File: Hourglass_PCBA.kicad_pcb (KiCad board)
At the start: 2 copper layers, 40.9 x 87.5 mm, 152 parts, among them J1 B2B-PH-SM4-TBLFSN, J2 UJ31-CH-G2-SMT-TR, J3 009159010061911, SW1 KMR221NGLFS, U1 STM32L432KCUx, U2 LP5860, U3 LSM6DSOXTR, U4 MCP1727T-3302E/SN, U5 BQ25185DLHR

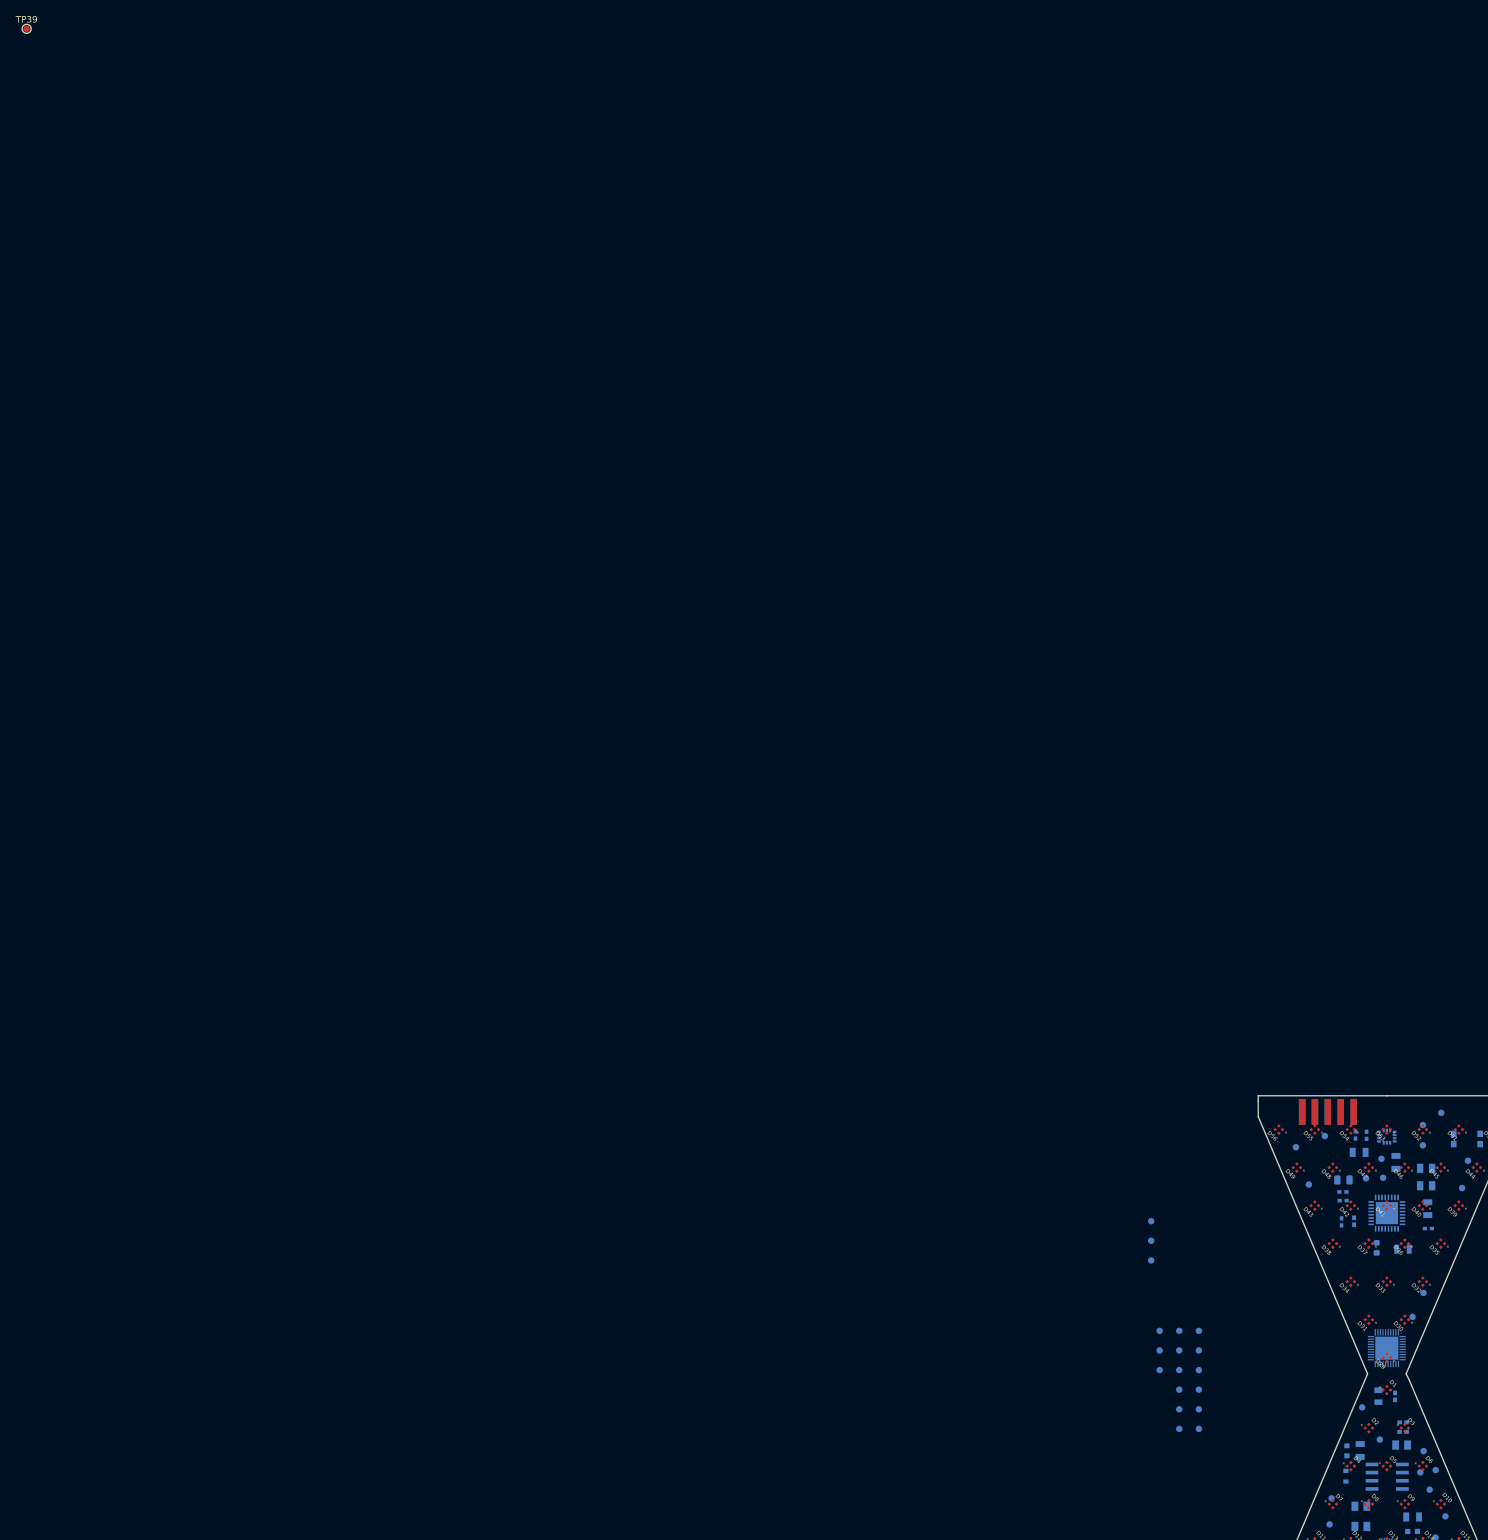
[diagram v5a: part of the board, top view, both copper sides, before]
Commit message: Updated the 3D models
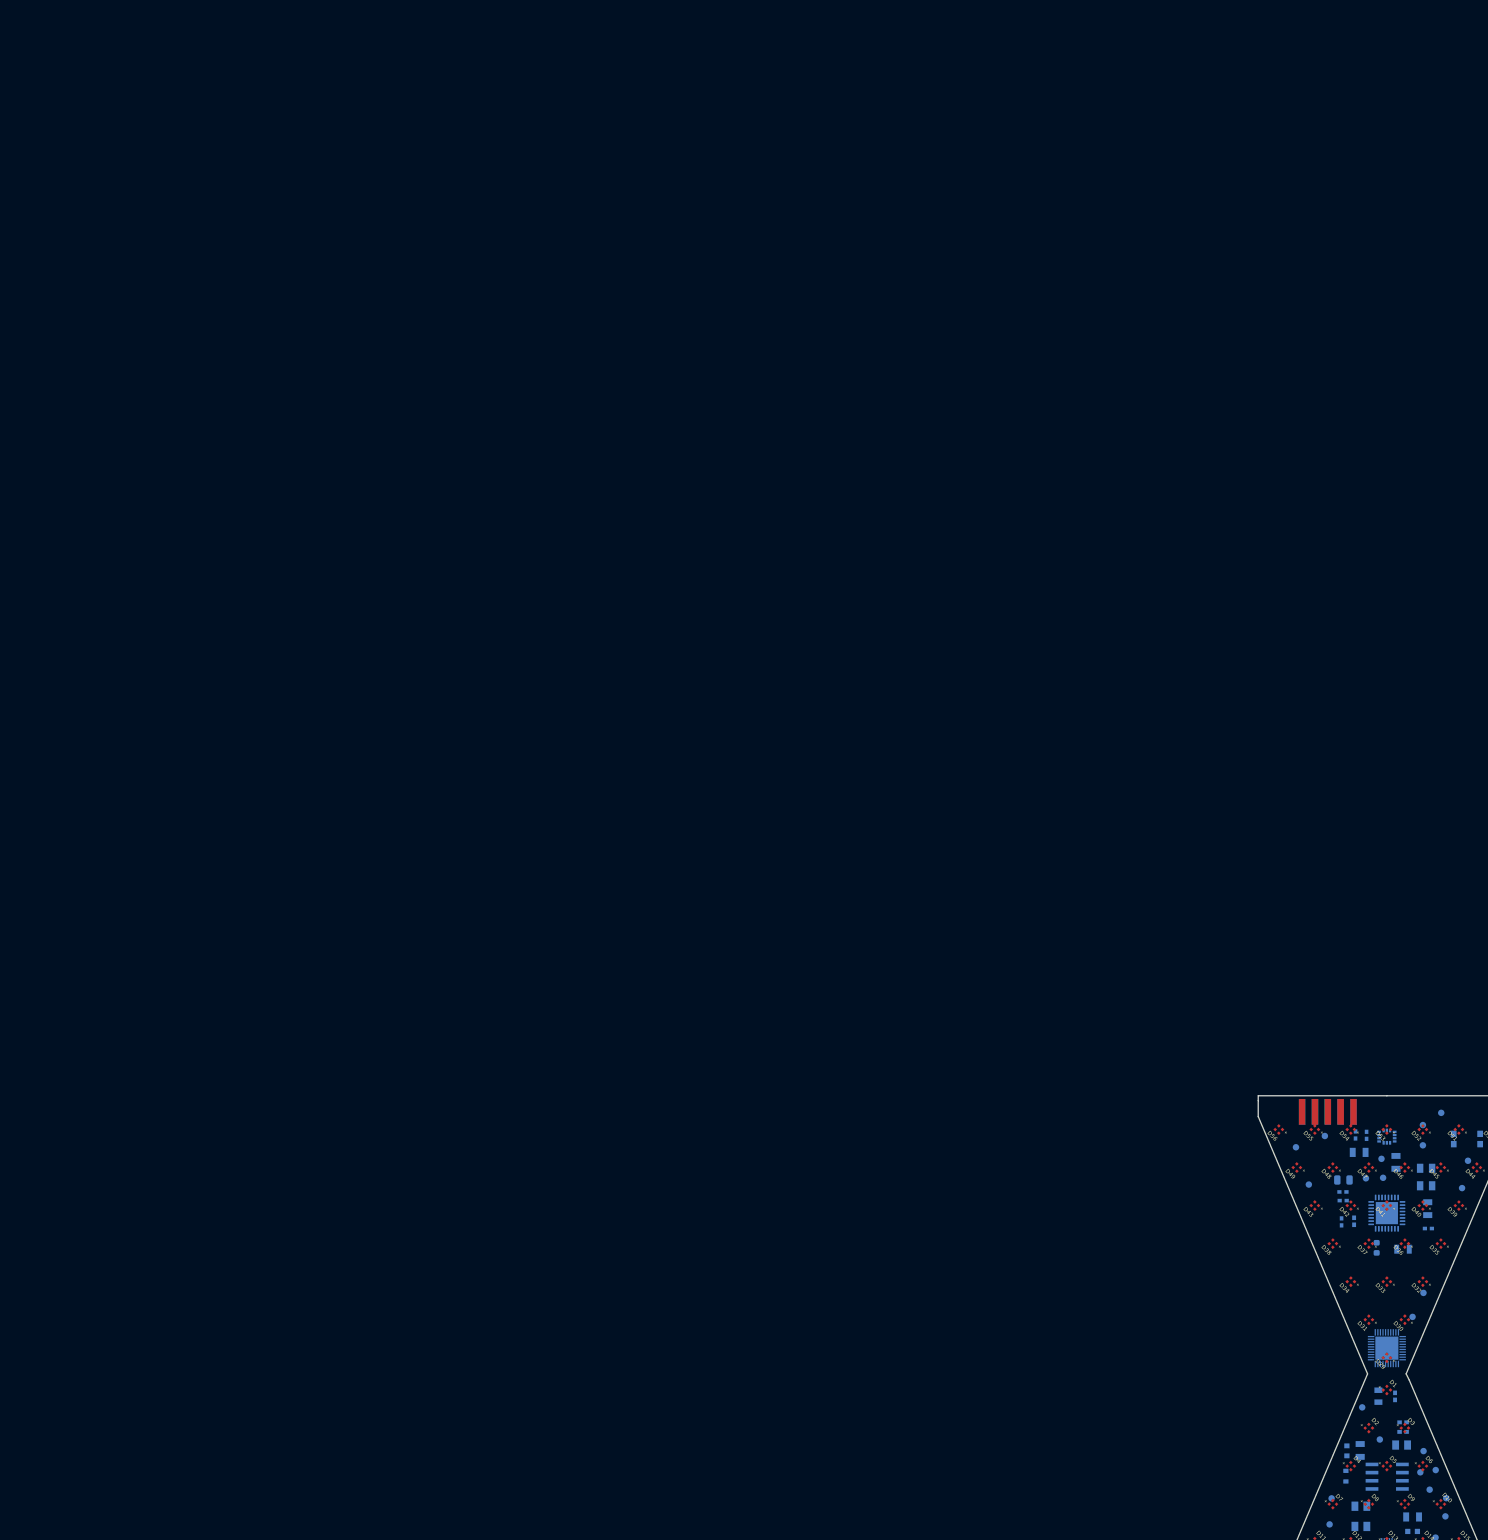
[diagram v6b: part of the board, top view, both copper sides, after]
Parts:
- removed TP10, TP11, TP12, TP13, TP14, TP15, TP16, TP17, TP18, TP19, TP20, TP21, TP22, TP23, TP6, TP7, TP8, TP9: TestPoint, TestPoint:TestPoint_Pad_D1.0mm
- TP39: moved to B.Cu
- moved TP39 317.7 mm to (209.2, 219.3)

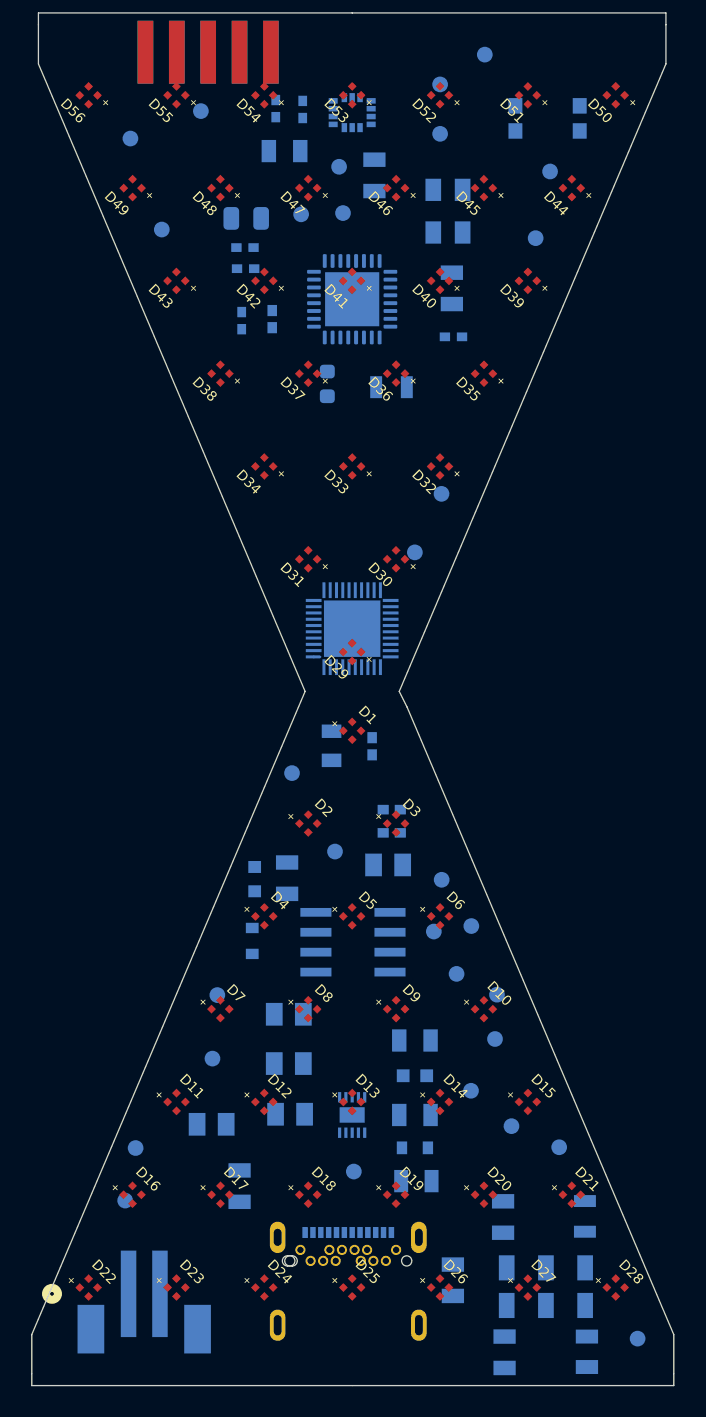
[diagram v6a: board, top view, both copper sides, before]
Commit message: Started routing all of the SW sides.
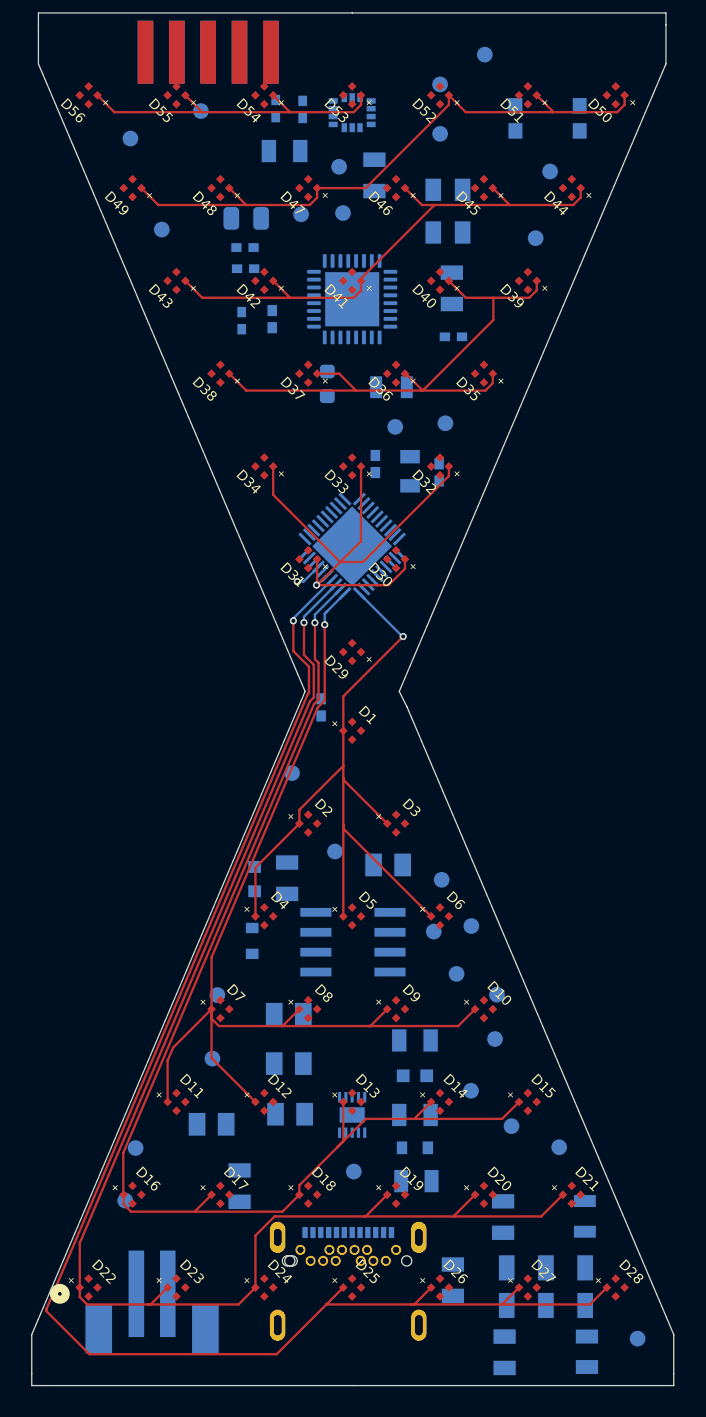
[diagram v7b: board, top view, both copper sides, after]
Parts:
- moved C7 21.7 mm to (205.5, 186.0), turned to 90 degrees
- moved C9 18.2 mm to (203.7, 186.0), turned to 90 degrees
- moved C10 18.0 mm to (201.5, 185.5), turned to 90 degrees
- moved C8 9.18 mm to (198.0, 201.0), turned to -90 degrees
- moved TP1 8.10 mm to (202.7, 183.1)
- moved U2 5.25 mm to (200.0, 190.8), turned to 135 degrees
- moved TP29 4.51 mm to (205.9, 182.9)
- moved J1 0.50 mm to (187.2, 239.6)
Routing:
- net /LED Driver +  LEDs/SW4: track 0.00 -> 94.9 mm, vias 0 -> 1
- net /LED Driver +  LEDs/SW3: track 0.00 -> 91.1 mm, vias 0 -> 1
- net /LED Driver +  LEDs/SW2: track 0.00 -> 77.3 mm, vias 0 -> 1
- net /LED Driver +  LEDs/SW1: track 0.00 -> 64.4 mm, vias 0 -> 1
- net /LED Driver +  LEDs/SW0: track 0.00 -> 47.5 mm, vias 0 -> 1
- net /LED Driver +  LEDs/SW8: track 0.00 -> 39.1 mm
- net /LED Driver +  LEDs/SW6: track 0.00 -> 38.9 mm, vias 0 -> 1
- net /LED Driver +  LEDs/SW5: track 0.00 -> 35.7 mm, vias 0 -> 1
- net /LED Driver +  LEDs/SW7: track 0.00 -> 34.7 mm
- net /LED Driver +  LEDs/SW9: track 0.00 -> 21.1 mm

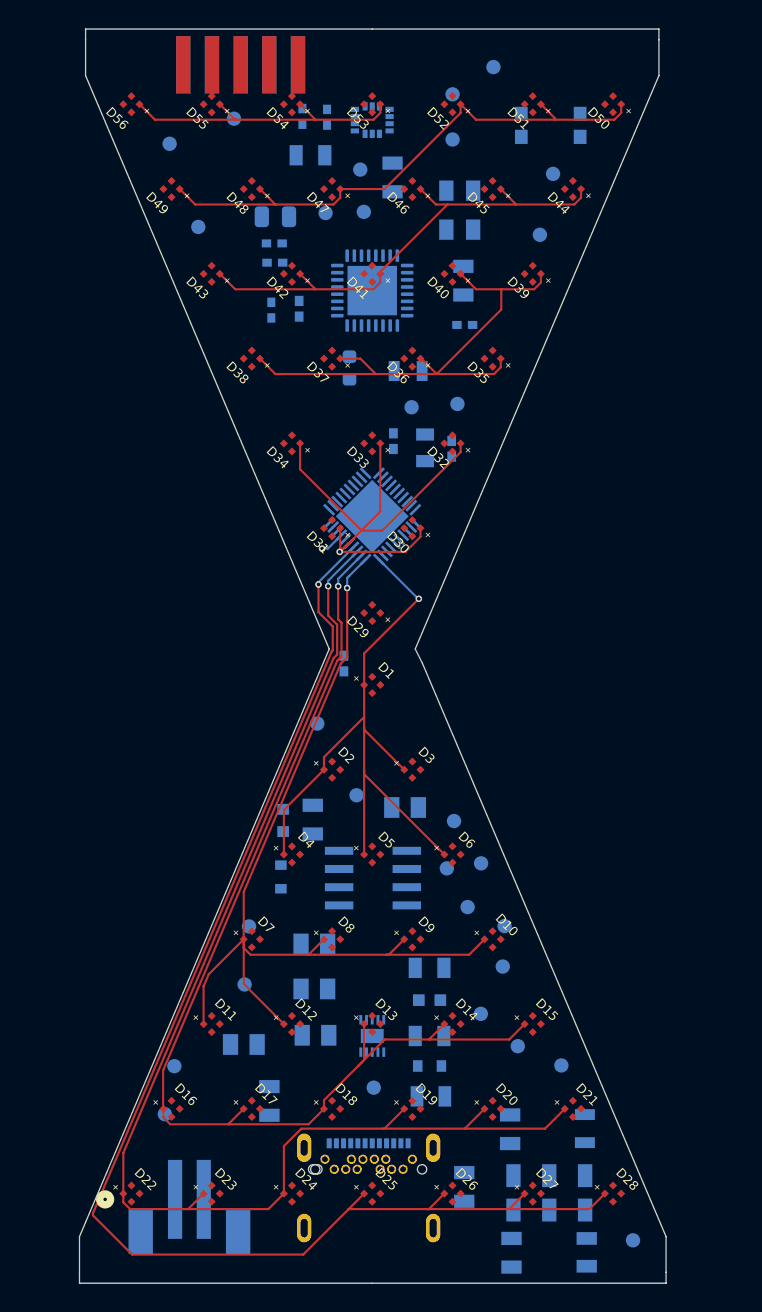
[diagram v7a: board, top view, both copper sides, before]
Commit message: Routed all of the SWx nets. Routing the CSx.
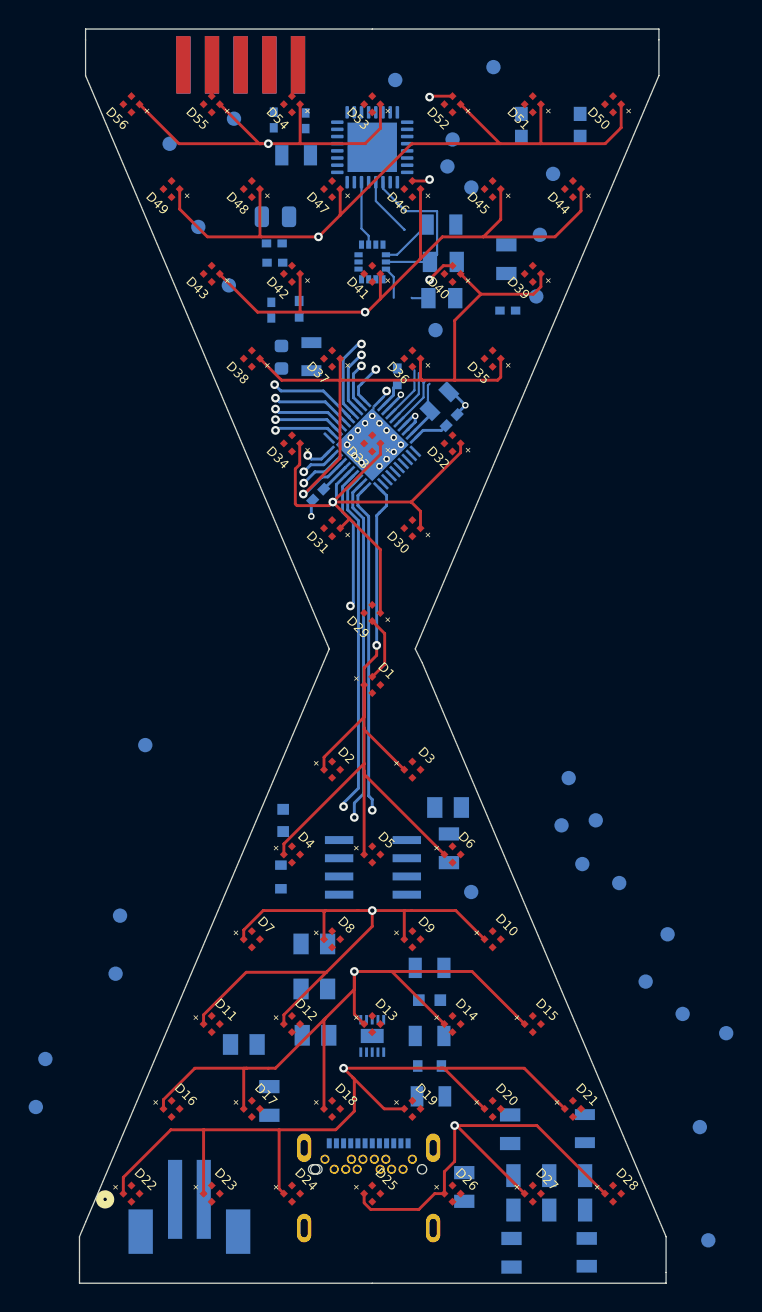
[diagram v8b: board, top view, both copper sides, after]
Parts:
- moved TP38 22.9 mm to (222.9, 233.4)
- moved TP1 15.3 mm to (190.0, 174.6)
- moved TP5 12.1 mm to (184.2, 206.7)
- moved C8 11.9 mm to (196.2, 189.2), turned to -135 degrees
- moved TP27 11.7 mm to (224.7, 226.8)
- moved TP37 11.7 mm to (220.6, 219.9)
- moved TP42 11.7 mm to (221.7, 225.5)
- moved TP48 11.7 mm to (219.1, 223.2)
- moved TP41 10.5 mm to (206.9, 217.0)
- moved U1 10.0 mm to (200.0, 165.0), turned to -90 degrees
- moved U3 9.89 mm to (200.0, 173.0), turned to 90 degrees
- moved R13 9.71 mm to (205.4, 213.9)
- moved TP4 9.65 mm to (204.4, 177.8)
- moved TP29 9.30 mm to (211.4, 175.4)
- moved TP2 9.10 mm to (205.2, 166.3)
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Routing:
- net /LED Driver +  LEDs/SW9: track 21.1 -> 51.6 mm, vias 0 -> 2
- net /LED Driver +  LEDs/SW8: track 39.1 -> 69.0 mm, vias 0 -> 2
- net /LED Driver +  LEDs/CS17: track 0.00 -> 28.4 mm, vias 0 -> 4
- net /LED Driver +  LEDs/SW7: track 34.7 -> 60.6 mm, vias 0 -> 2
- net /LED Driver +  LEDs/I2C.SCL: track 0.00 -> 15.5 mm
- net /LED Driver +  LEDs/I2C.SDA: track 0.00 -> 11.3 mm
- net /LED Driver +  LEDs/SW4: track 94.9 -> 84.3 mm, vias 1 -> 2
- net /LED Driver +  LEDs/SW1: track 64.4 -> 74.2 mm, vias 1 -> 2
- net /LED Driver +  LEDs/SW6: track 38.9 -> 48.5 mm
- net GND: track 0.00 -> 8.56 mm, vias 0 -> 19
- net /LED Driver +  LEDs/SW2: track 77.3 -> 85.3 mm, vias 1 -> 2
- net /LED Driver +  LEDs/SW3: track 91.1 -> 99.0 mm, vias 1 -> 2
- net /LED Driver +  LEDs/SW0: track 47.5 -> 54.4 mm
- net /LED Driver +  LEDs/CS13: track 0.00 -> 6.21 mm, vias 0 -> 1
- net /LED Driver +  LEDs/CS14: track 0.00 -> 5.82 mm, vias 0 -> 1
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- added copper zone on In2.Cu, net GND
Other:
- copper layers 2 -> 4
